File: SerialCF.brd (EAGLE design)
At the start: 101.6 x 50.5 mm, 13 parts, among them IC1 XR-16C550P, T1 BC547

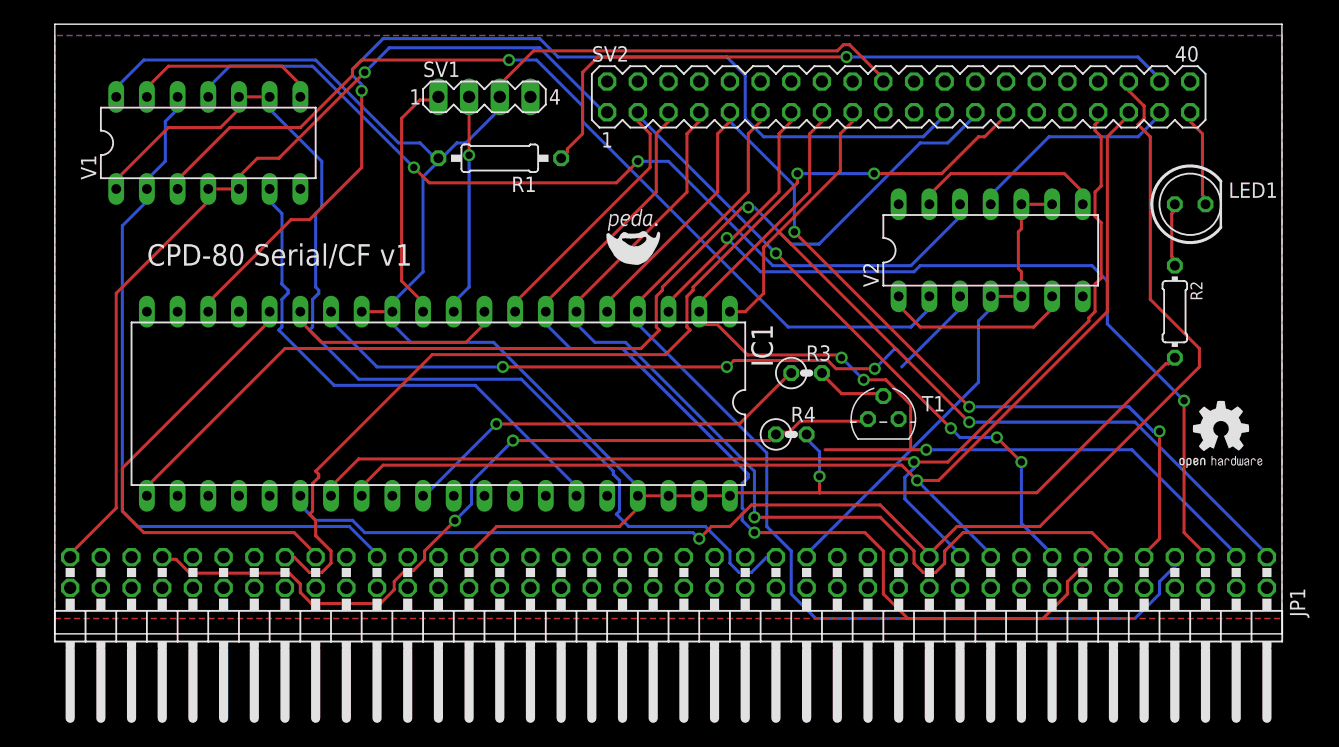
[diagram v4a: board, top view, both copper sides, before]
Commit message: Add Decoupling Capacitors.
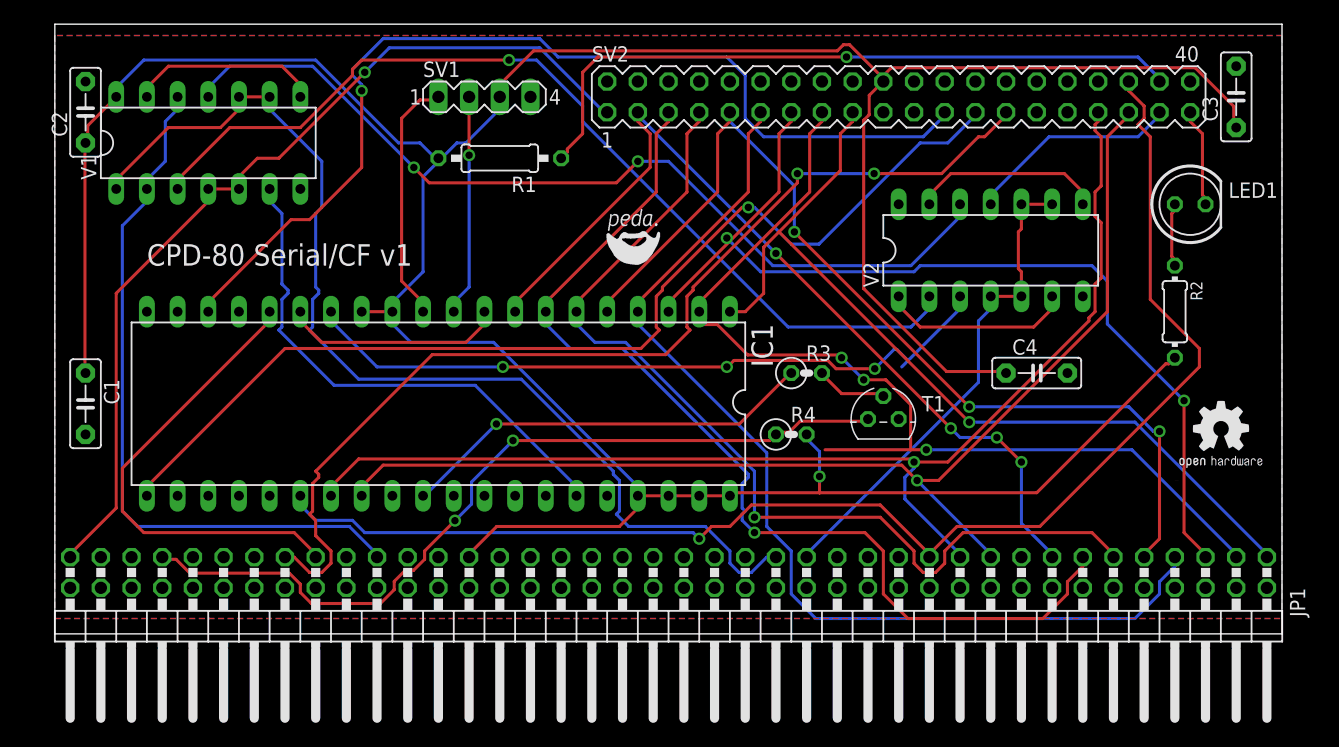
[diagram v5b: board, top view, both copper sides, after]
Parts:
- added C1, C2, C3, C4: 0.1µF, capacitor-wima:C5B2.5
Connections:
- net GND: now also C1.2, C2.2, C3.2, C4.2
- net VCC: now also C1.1, C2.1, C3.1, C4.1
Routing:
- net VCC: track 191.0 -> 280.5 mm
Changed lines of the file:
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@@
 <element name="R3" library="resistor" package="0207/2V" value="100k" x="64.77" y="21.59"/>
 <element name="R4" library="resistor" package="0207/2V" value="3.3k" x="63.5" y="16.51"/>
+<element name="C1" library="capacitor-wima" package="C5B2.5" value="0.1µF" x="5.08" y="19.05" rot="R270"/>
+<element name="C2" library="capacitor-wima" package="C5B2.5" value="0.1µF" x="5.08" y="43.18" rot="R90"/>
+<element name="C3" library="capacitor-wima" package="C5B2.5" value="0.1µF" x="100.33" y="44.45" rot="R90"/>
+<element name="C4" library="capacitor-wima" package="C5B2.5" value="0.1µF" x="83.82" y="21.59"/>
 </elements>
 <signals>
@@
 <wire x1="65.8368" y1="11.6586" x2="65.8368" y2="11.684" width="0.254" layer="1"/>
 <via x="65.8368" y="13.0302" extent="1-16" drill="0.6096"/>
+<contactref element="C1" pad="1"/>
+<contactref element="C2" pad="1"/>
+<contactref element="C3" pad="1"/>
+<contactref element="C4" pad="1"/>
+<wire x1="5.0292" y1="40.4622" x2="5.0292" y2="21.717" width="0.254" layer="1"/>
+<wire x1="5.0292" y1="21.717" x2="5.08" y2="21.59" width="0.254" layer="1"/>
+<wire x1="5.0292" y1="40.4622" x2="5.08" y2="40.64" width="0.254" layer="1"/>
+<wire x1="76.3524" y1="21.717" x2="81.153" y2="21.717" width="0.254" layer="1"/>
+<wire x1="69.4944" y1="28.575" x2="76.3524" y2="21.717" width="0.254" layer="1"/>
+<wire x1="69.4944" y1="42.5196" x2="69.4944" y2="28.575" width="0.254" layer="1"/>
+<wire x1="69.9516" y1="42.9768" x2="69.4944" y2="42.5196" width="0.254" layer="1"/>
+<wire x1="69.9516" y1="44.577" x2="69.9516" y2="42.9768" width="0.254" layer="1"/>
+<wire x1="71.0946" y1="45.72" x2="69.9516" y2="44.577" width="0.254" layer="1"/>
+<wire x1="81.153" y1="21.717" x2="81.28" y2="21.59" width="0.254" layer="1"/>
+<wire x1="71.0946" y1="45.72" x2="71.12" y2="45.72" width="0.254" layer="1"/>
+<wire x1="100.1268" y1="43.6626" x2="100.1268" y2="42.0624" width="0.254" layer="1"/>
+<wire x1="96.9264" y1="46.863" x2="100.1268" y2="43.6626" width="0.254" layer="1"/>
+<wire x1="71.7804" y1="46.863" x2="96.9264" y2="46.863" width="0.254" layer="1"/>
+<wire x1="71.0946" y1="46.1772" x2="71.7804" y2="46.863" width="0.254" layer="1"/>
+<wire x1="100.1268" y1="42.0624" x2="100.33" y2="41.91" width="0.254" layer="1"/>
+<wire x1="71.0946" y1="46.1772" x2="71.12" y2="45.72" width="0.254" layer="1"/>
+<wire x1="5.2578" y1="42.0624" x2="5.2578" y2="40.6908" width="0.254" layer="1"/>
+<wire x1="7.5438" y1="44.3484" x2="5.2578" y2="42.0624" width="0.254" layer="1"/>
+<wire x1="5.2578" y1="40.6908" x2="5.08" y2="40.64" width="0.254" layer="1"/>
+<wire x1="7.5438" y1="44.3484" x2="7.62" y2="44.45" width="0.254" layer="1"/>
 </signal>
 <signal name="GND">
@@
 </polygon>
 <contactref element="T1" pad="1"/>
+<contactref element="C1" pad="2"/>
+<contactref element="C2" pad="2"/>
+<contactref element="C3" pad="2"/>
+<contactref element="C4" pad="2"/>
 </signal>
 <signal name="A0">

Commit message: Change addressbus to allow more devices on it.
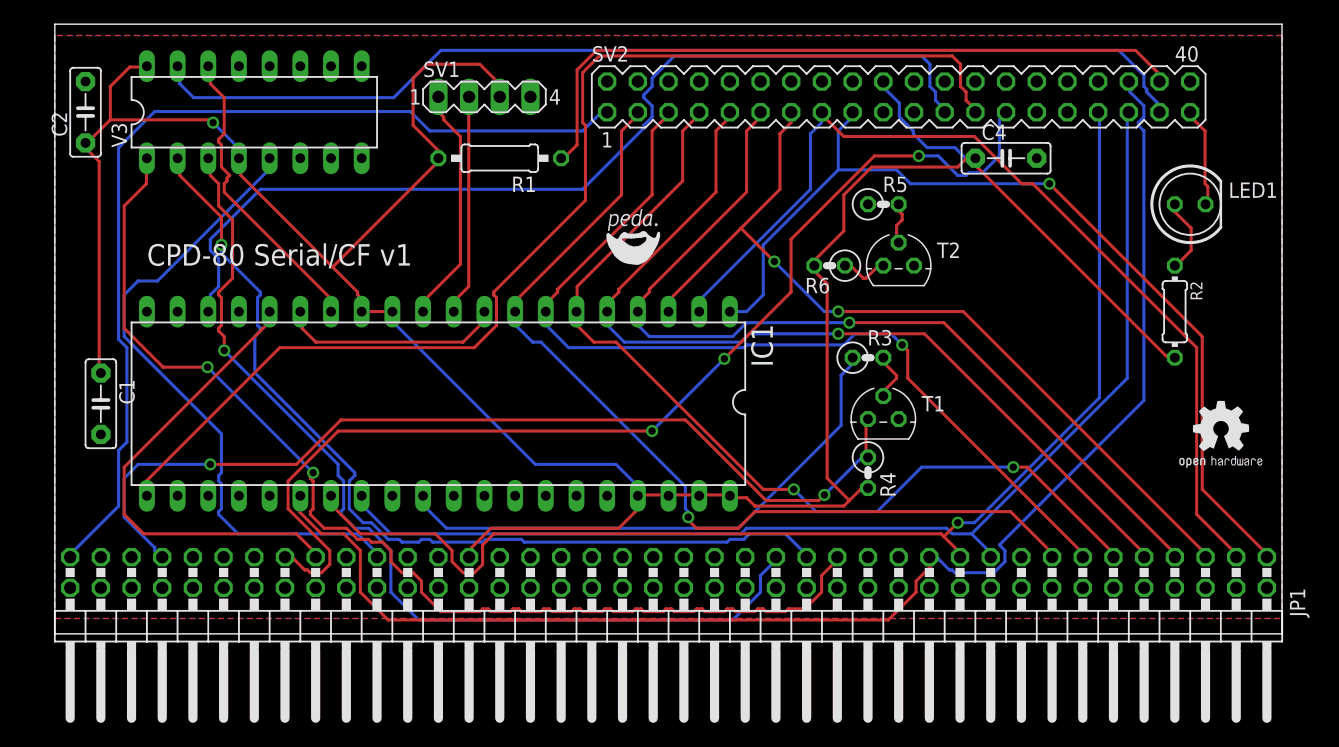
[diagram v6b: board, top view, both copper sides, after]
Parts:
- removed C3: 0.1µF, capacitor-wima:C5B2.5
- removed V1, V2: 74HC00N, 74ttl-din:DIL14
- added R5: 100k, resistor:0207/2V
- added R6: 3.3k, resistor:0207/2V
- added T2: BC547, transistor:TO92
- added V3: 74138N, 74ttl-din:DIL16
- moved C4 18.0 mm to (81.3, 39.4)
- moved R4 7.10 mm to (69.8, 13.3), turned to 270 degrees
- moved R3 5.24 mm to (69.8, 22.9)
- moved C1 1.27 mm to (6.35, 19.1)
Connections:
- removed net +UB: V2.14
- removed net -UB: V2.7
- removed net N$17: V1.13, V1.8
- removed net N$18: IC1.14, V2.3
- removed net N$19: JP1.59, V1.12, V1.2
- net !RESET: no longer V1.4, V1.5
- net A5: now also V3.1
- net A6: now also V3.2; no longer V2.10, V2.4, V2.5, V2.9
- net A7: now also V3.3; no longer V1.1, V1.10, V1.9
- net GND: now also T2.1, V3.6, V3.8; no longer C3.2, V1.7
- net IOCS1: now also V3.15; no longer V2.11
- net N$4: now also IC1.14, V3.14; no longer V1.3, V2.2
- net N$5: now also JP1.59, V3.5; no longer V2.1, V2.6
- net N$6: now also R5.2, T2.2; no longer V2.13, V2.8
- net N$7: now also R6.1, T2.3; no longer V1.11, V2.12
- net RESET: no longer V1.6
- net VCC: now also R6.2, V3.16, V3.4; no longer C3.1, V1.14
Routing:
- net A5: track 0.00 -> 92.0 mm, vias 0 -> 2
- net N$7: track 74.7 -> 4.06 mm, vias 2 -> 0
- net IOCS1: track 17.7 -> 88.0 mm
- net N$18: track 59.5 -> 0.00 mm, vias 3 -> 0
- net N$19: track 59.0 -> 0.00 mm
- net N$4: track 78.9 -> 25.4 mm, vias 1 -> 0
- net VCC: track 280.5 -> 230.4 mm
- net RESET: track 43.4 -> 0.00 mm
- net N$5: track 15.8 -> 53.8 mm
- net A6: track 40.8 -> 76.6 mm, vias 0 -> 1
- net N$17: track 15.8 -> 0.00 mm
- net N$6: track 15.8 -> 3.60 mm
- net N$10: track 34.7 -> 45.7 mm, vias 1 -> 0
- net N$9: track 68.7 -> 79.0 mm
- net D2: track 80.7 -> 70.6 mm
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
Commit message: Add Ground Rail to JEANNECTOR
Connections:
- net GND: now also JP1.10, JP1.12, JP1.14, JP1.16, JP1.18, JP1.2, JP1.20, JP1.22, JP1.24, JP1.26, JP1.28, JP1.30, JP1.32, JP1.34, JP1.36, JP1.38, JP1.4, JP1.40, JP1.42, JP1.44, JP1.46, JP1.48, JP1.50, JP1.52, JP1.54, JP1.56, JP1.58, JP1.6, JP1.60, JP1.62, JP1.64, JP1.66, JP1.68, JP1.70, JP1.72, JP1.74, JP1.76, JP1.78, JP1.8, JP1.80
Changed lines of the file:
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@@
 <contactref element="V3" pad="6"/>
 <contactref element="T2" pad="1"/>
+<contactref element="JP1" pad="2"/>
+<contactref element="JP1" pad="4"/>
+<contactref element="JP1" pad="6"/>
+<contactref element="JP1" pad="8"/>
+<contactref element="JP1" pad="10"/>
+<contactref element="JP1" pad="12"/>
+<contactref element="JP1" pad="14"/>
+<contactref element="JP1" pad="16"/>
+<contactref element="JP1" pad="18"/>
+<contactref element="JP1" pad="20"/>
+<contactref element="JP1" pad="22"/>
+<contactref element="JP1" pad="24"/>
+<contactref element="JP1" pad="26"/>
+<contactref element="JP1" pad="28"/>
+<contactref element="JP1" pad="30"/>
+<contactref element="JP1" pad="32"/>
+<contactref element="JP1" pad="34"/>
+<contactref element="JP1" pad="36"/>
+<contactref element="JP1" pad="38"/>
+<contactref element="JP1" pad="40"/>
+<contactref element="JP1" pad="42"/>
+<contactref element="JP1" pad="44"/>
+<contactref element="JP1" pad="46"/>
+<contactref element="JP1" pad="48"/>
+<contactref element="JP1" pad="50"/>
+<contactref element="JP1" pad="52"/>
+<contactref element="JP1" pad="54"/>
+<contactref element="JP1" pad="56"/>
+<contactref element="JP1" pad="58"/>
+<contactref element="JP1" pad="60"/>
+<contactref element="JP1" pad="62"/>
+<contactref element="JP1" pad="64"/>
+<contactref element="JP1" pad="66"/>
+<contactref element="JP1" pad="68"/>
+<contactref element="JP1" pad="70"/>
+<contactref element="JP1" pad="72"/>
+<contactref element="JP1" pad="74"/>
+<contactref element="JP1" pad="76"/>
+<contactref element="JP1" pad="78"/>
+<contactref element="JP1" pad="80"/>
 </signal>
 <signal name="A0">

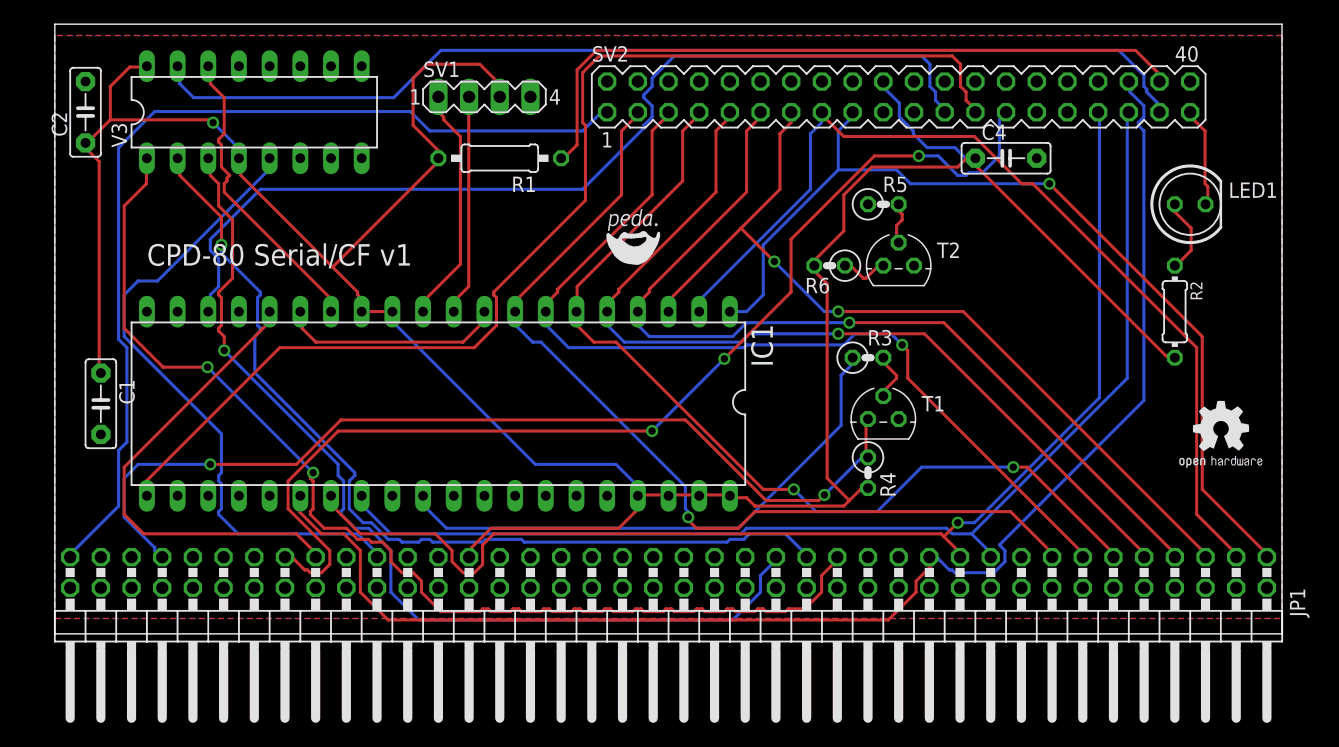
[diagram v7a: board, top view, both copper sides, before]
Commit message: Make Top Plane a VCC Plane instead of Ground, add Holes
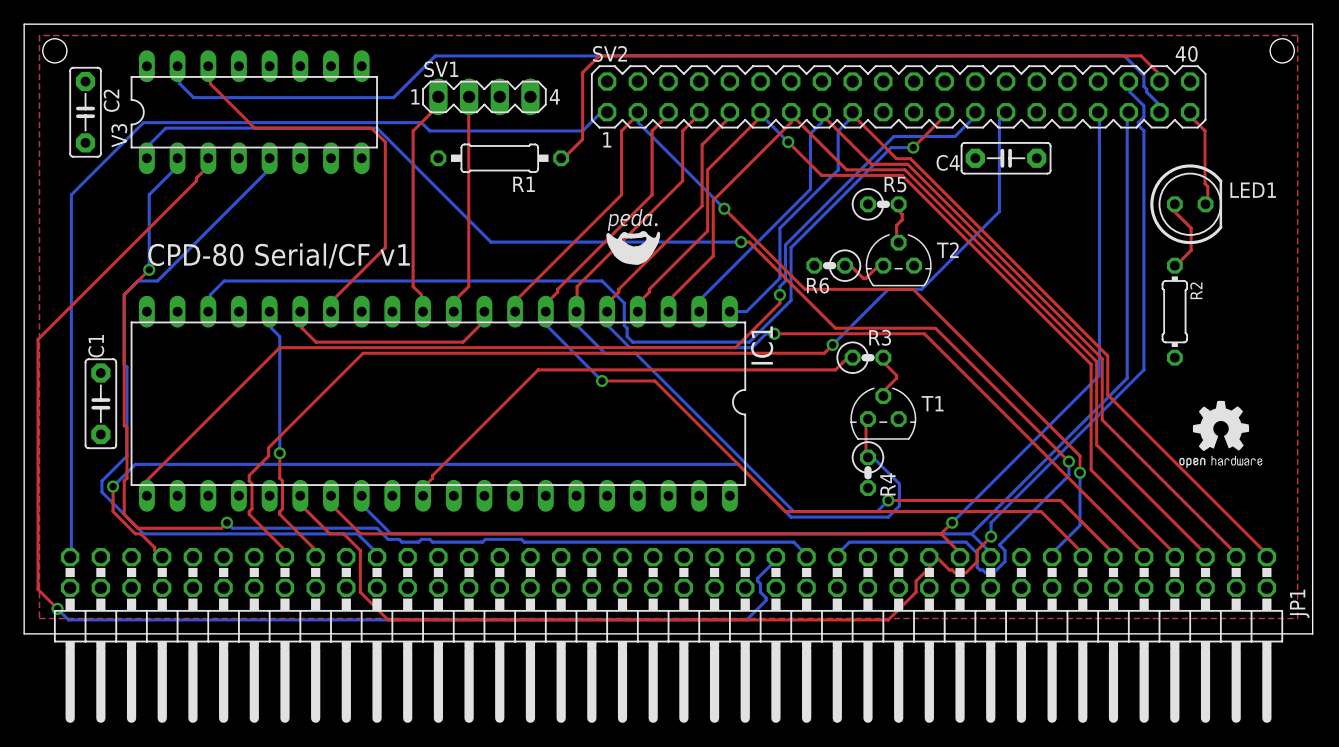
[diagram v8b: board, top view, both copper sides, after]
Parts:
- turned C2 to 270 degrees
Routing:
- net VCC: track 230.4 -> 0.00 mm, vias 1 -> 0
- net A7: track 80.3 -> 108.1 mm
- net A5: track 92.0 -> 117.0 mm
- net N$1: track 39.3 -> 22.1 mm, vias 0 -> 1
- net A6: track 76.6 -> 90.4 mm, vias 1 -> 2
- net !RD: track 96.6 -> 85.4 mm, vias 0 -> 1
- net N$4: track 25.4 -> 34.0 mm
- net N$5: track 53.8 -> 59.7 mm
- net N$9: track 79.0 -> 84.6 mm, vias 2 -> 1
- net D1: track 78.6 -> 73.5 mm
- net A1: track 100.3 -> 95.2 mm
- net N$10: track 45.7 -> 40.8 mm
- net D0: track 78.0 -> 73.4 mm, vias 1 -> 0
- net D2: track 70.6 -> 74.4 mm, vias 2 -> 0
- net !WR: track 80.1 -> 77.2 mm, vias 0 -> 1
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- added copper zone on layer 1, net VCC
- removed copper zone on layer 1, net GND
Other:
- board size 101.6 x 50.5 mm -> 106.7 x 50.5 mm
